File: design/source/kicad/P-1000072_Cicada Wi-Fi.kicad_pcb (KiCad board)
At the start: 2 copper layers, 40 x 65 mm, 66 parts, among them J3 Host, U1 HX3406, U3 ESP-07S

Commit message: deleted previous production files, reviewed SCH and PCB files
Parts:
- added TP10: GND, okra-footprints:TestPoint_Pad_D1.5mm, B.Cu at (139.2, 81.5)
- R13: value 22.6K -> 340k
- TP4: value EN -> VCC; moved to B.Cu
- TP7: value Vcc -> VCC
- moved TP4 29.2 mm to (136.0, 81.7)
- moved TP5 23.2 mm to (134.6, 80.1)
- moved TP7 22.9 mm to (135.6, 80.7), turned to 90 degrees
- moved TP23 0.79 mm to (131.8, 81.3)
- moved R11 0.69 mm to (123.2, 77.5)
- moved C29 0.63 mm to (122.3, 78.7)
- moved TP28 0.53 mm to (121.3, 77.2)
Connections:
- R12 pad 1: /3V3 -> /Vref(3V3)
- R13 pad 1: /3V3 -> /Vref(3V3)
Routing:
- net /Vref(3V3): track 0.00 -> 9.94 mm, vias 0 -> 1
- net /3V3: track 41.3 -> 36.9 mm, vias 3 -> 2
- net /RST: track 101.5 -> 99.3 mm
- net GND: track 54.9 -> 56.0 mm, vias 219 -> 224
- net /5V0: track 64.4 -> 65.0 mm, vias 5 -> 2
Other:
- board text added: "P-1000072-V4"
- board text removed: "P-1000072-V6"

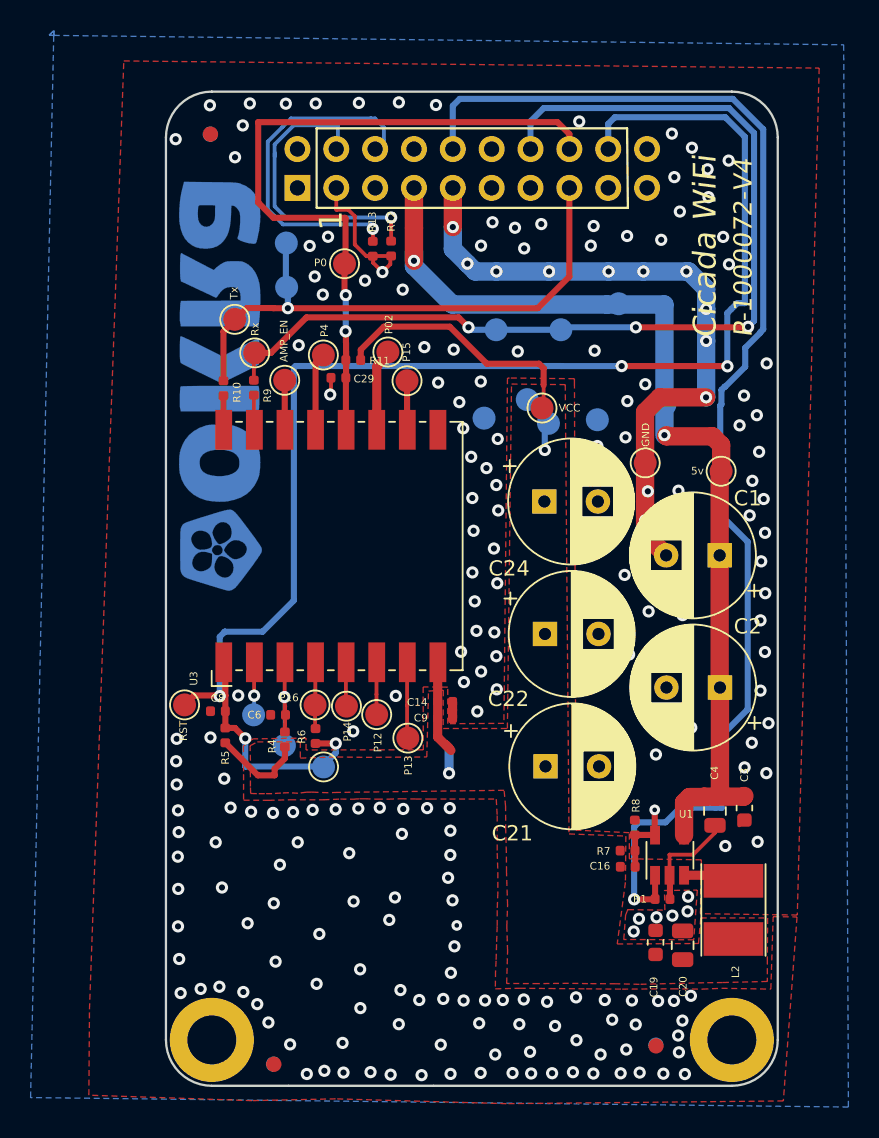
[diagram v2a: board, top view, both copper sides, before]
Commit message: 1.Schematics improvement and crediblity (cleared empty spaces, improved read me and reviewed and cleaned component spec mismatch 2.PCB improments (cleaned top layer copper zones, cleaned vias and updated production release verion on the pcb silk screen 3.BOM mismatch (R13 changed to output board version number 6.3, previously R13 was DNP)
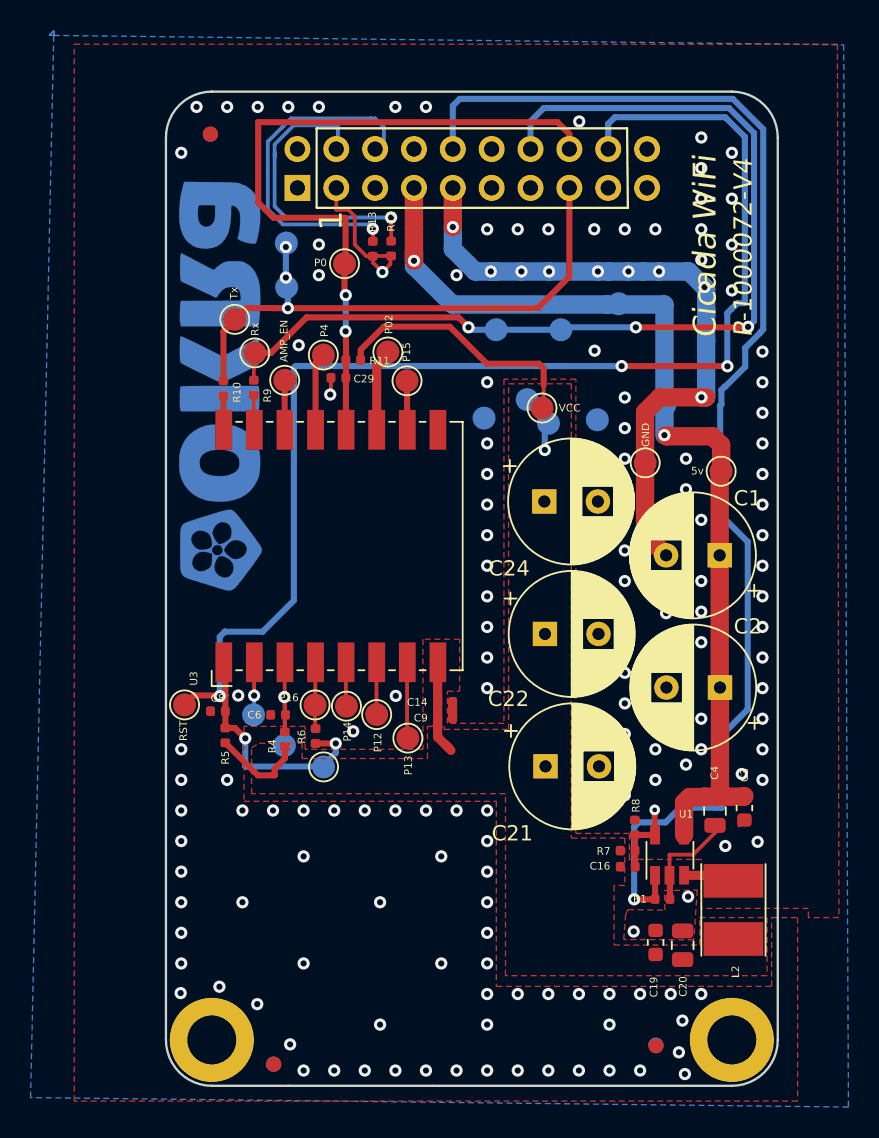
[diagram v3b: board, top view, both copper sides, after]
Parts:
- R13: value 340k -> 86.6k
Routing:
- net /3V3: track 36.9 -> 35.2 mm, vias 2 -> 1
- net GND: vias 224 -> 158
- net /UART_TX_3v3: vias 1 -> 3
